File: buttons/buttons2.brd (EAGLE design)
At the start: 73 x 44 mm, 14 parts, among them U1 attiny2313

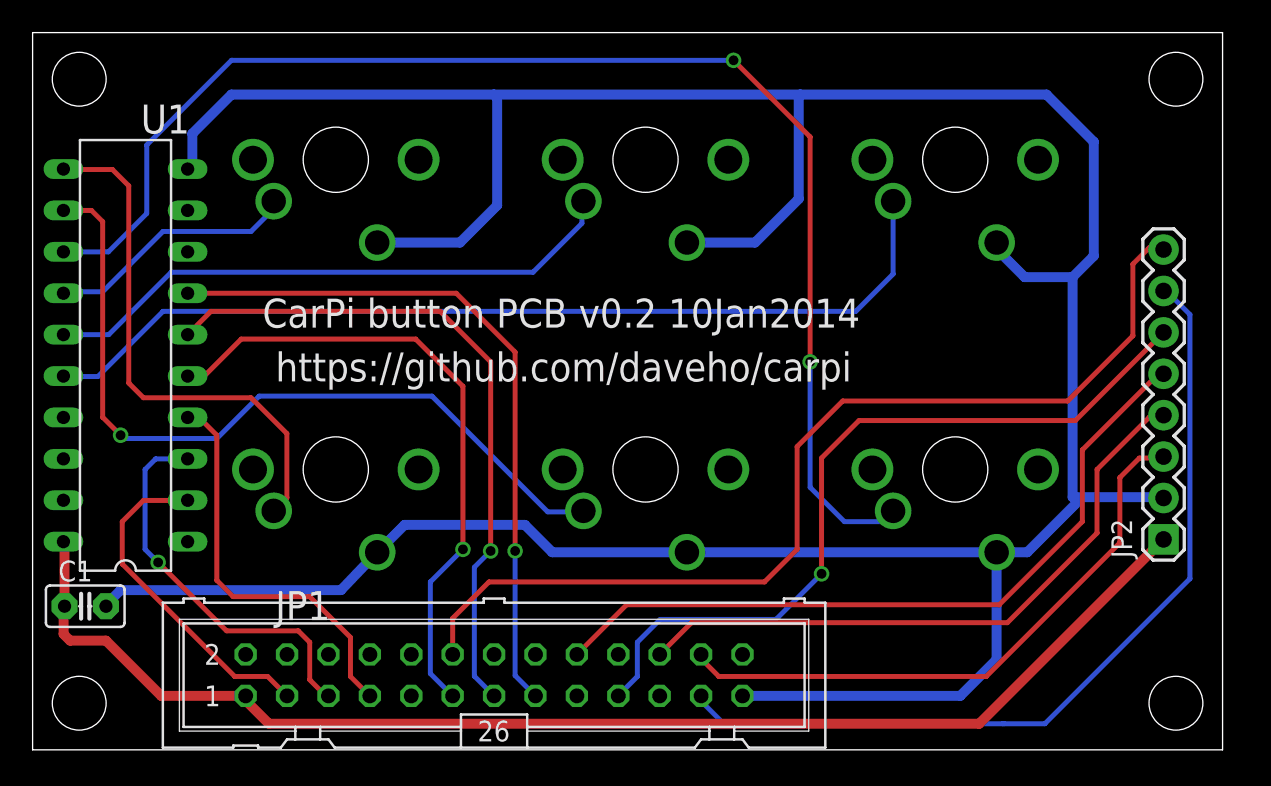
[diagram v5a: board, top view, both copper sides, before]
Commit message: updated buttons2/plate drawing for 19mm keycap
Made the PCB 74mm rather than 73mm to allow more space
between button cutout and button PCB screw hole.
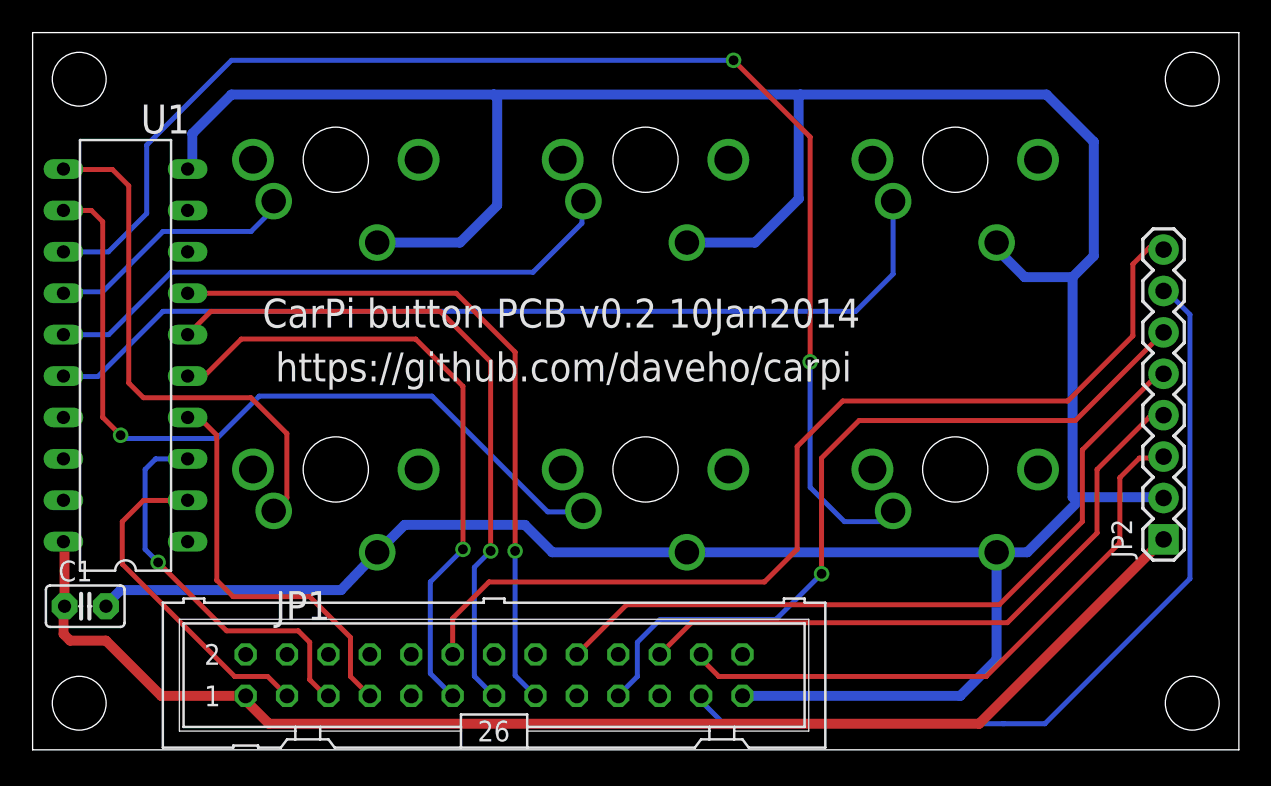
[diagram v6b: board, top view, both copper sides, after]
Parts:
- moved STANDOFF1 1.00 mm to (71.1, 2.86)
- moved STANDOFF3 1.00 mm to (71.1, 41.1)
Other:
- board size 73 x 44 mm -> 74 x 44 mm
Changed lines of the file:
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@@
 <board>
 <plain>
-<wire x1="0" y1="0" x2="73" y2="0" width="0" layer="20"/>
-<wire x1="73" y1="0" x2="73" y2="44" width="0" layer="20"/>
-<wire x1="73" y1="44" x2="0" y2="44" width="0" layer="20"/>
+<wire x1="0" y1="0" x2="74" y2="0" width="0" layer="20"/>
+<wire x1="74" y1="0" x2="74" y2="44" width="0" layer="20"/>
+<wire x1="74" y1="44" x2="0" y2="44" width="0" layer="20"/>
 <wire x1="0" y1="44" x2="0" y2="0" width="0" layer="20"/>
 <text x="14.1" y="25.9" size="1.778" layer="21" font="vector">CarPi button PCB v0.2 10Jan2014</text>
@@
 <attribute name="VALUE" x="0.679" y="6.016" size="1.27" layer="27" font="vector" ratio="10"/>
 </element>
-<element name="STANDOFF1" library="SparkFun-Electromechanical" package="STAND-OFF" value="STAND-OFF" x="70.14" y="2.86"/>
+<element name="STANDOFF1" library="SparkFun-Electromechanical" package="STAND-OFF" value="STAND-OFF" x="71.14" y="2.86"/>
 <element name="STANDOFF2" library="SparkFun-Electromechanical" package="STAND-OFF" value="STAND-OFF" x="2.86" y="2.86"/>
-<element name="STANDOFF3" library="SparkFun-Electromechanical" package="STAND-OFF" value="STAND-OFF" x="70.14" y="41.14"/>
+<element name="STANDOFF3" library="SparkFun-Electromechanical" package="STAND-OFF" value="STAND-OFF" x="71.14" y="41.14"/>
 <element name="STANDOFF4" library="SparkFun-Electromechanical" package="STAND-OFF" value="STAND-OFF" x="2.86" y="41.14"/>
 <element name="S1" library="cherrymx" package="CHERRY-MX-I" value="CHERRY-MX-I" x="18.6" y="17.2" rot="MR180"/>
@@
 <wire x1="5.4" y1="19.3" x2="5.6" y2="19.1" width="0.3048" layer="16"/>
 <wire x1="5.6" y1="19.1" x2="11.3" y2="19.1" width="0.3048" layer="16"/>
-<wire x1="11.3" y1="19.1" x2="13.1" y2="19.1" width="0" layer="19" extent="1-16"/>
 <wire x1="24.5" y1="21.7" x2="31.6" y2="14.6" width="0.3048" layer="16"/>
 <wire x1="31.6" y1="14.6" x2="33.73" y2="14.6" width="0.3048" layer="16"/>

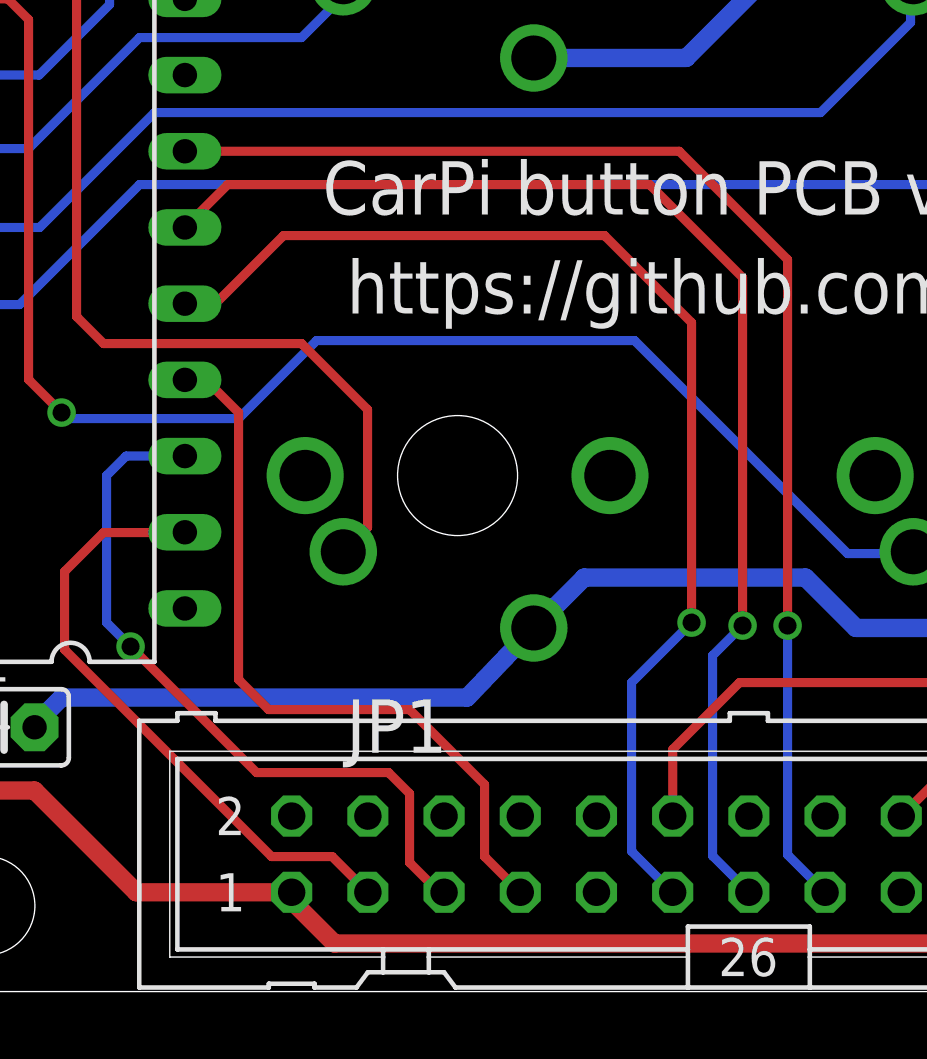
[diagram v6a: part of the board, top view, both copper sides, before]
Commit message: eliminated an unnecessary via
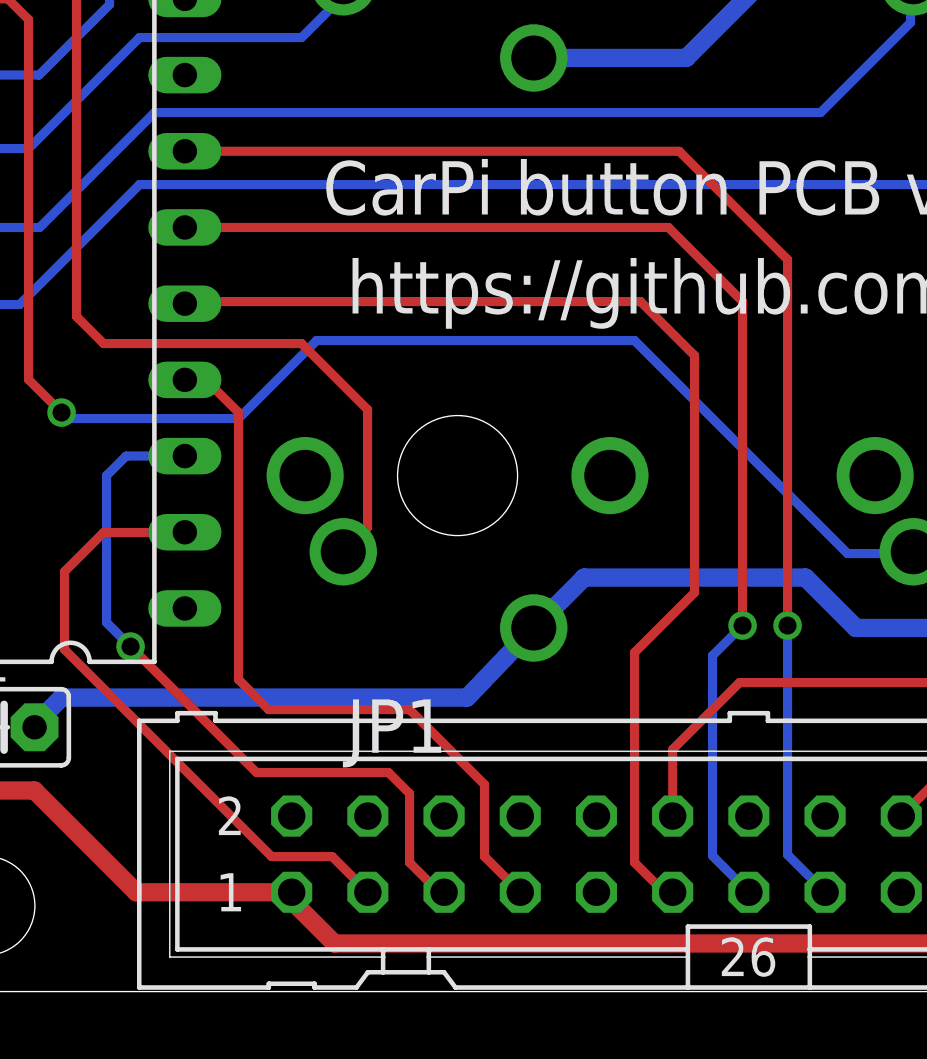
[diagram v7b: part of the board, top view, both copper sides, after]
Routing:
- net BUTTON4: track 39.4 -> 37.2 mm, vias 1 -> 0
- net BUTTON5: track 41.9 -> 40.2 mm
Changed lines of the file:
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@@
 <contactref element="JP1" pad="11"/>
 <contactref element="U1" pad="5"/>
-<wire x1="25.77" y1="3.31" x2="24.4" y2="4.68" width="0.3048" layer="16"/>
-<wire x1="24.4" y1="4.68" x2="24.4" y2="10.3" width="0.3048" layer="16"/>
-<wire x1="24.4" y1="10.3" x2="26.4" y2="12.3" width="0.3048" layer="16"/>
-<via x="26.4" y="12.3" extent="1-16" drill="0.6"/>
-<wire x1="9.51" y1="22.93" x2="10.53" y2="22.93" width="0.3048" layer="1"/>
-<wire x1="10.53" y1="22.93" x2="12.8" y2="25.2" width="0.3048" layer="1"/>
-<wire x1="12.8" y1="25.2" x2="23.5" y2="25.2" width="0.3048" layer="1"/>
-<wire x1="23.5" y1="25.2" x2="26.4" y2="22.3" width="0.3048" layer="1"/>
-<wire x1="26.4" y1="22.3" x2="26.4" y2="12.3" width="0.3048" layer="1"/>
+<wire x1="9.51" y1="22.93" x2="9.51" y2="22.99" width="0.3048" layer="1"/>
+<wire x1="9.51" y1="22.99" x2="9.5" y2="23" width="0.3048" layer="1"/>
+<wire x1="9.5" y1="23" x2="24.7" y2="23" width="0.3048" layer="1"/>
+<wire x1="24.7" y1="23" x2="26.5" y2="21.2" width="0.3048" layer="1"/>
+<wire x1="26.5" y1="21.2" x2="26.5" y2="13.3" width="0.3048" layer="1"/>
+<wire x1="25.77" y1="3.31" x2="25.49" y2="3.31" width="0.3048" layer="1"/>
+<wire x1="25.49" y1="3.31" x2="24.5" y2="4.3" width="0.3048" layer="1"/>
+<wire x1="24.5" y1="4.3" x2="24.5" y2="11.3" width="0.3048" layer="1"/>
+<wire x1="24.5" y1="11.3" x2="26.5" y2="13.3" width="0.3048" layer="1"/>
 </signal>
 <signal name="BUTTON5">
@@
 <wire x1="27.1" y1="11.2" x2="28.1" y2="12.2" width="0.3048" layer="16"/>
 <via x="28.1" y="12.2" extent="1-16" drill="0.6"/>
-<wire x1="9.51" y1="25.47" x2="10.94" y2="26.9" width="0.3048" layer="1"/>
-<wire x1="10.94" y1="26.9" x2="25" y2="26.9" width="0.3048" layer="1"/>
-<wire x1="25" y1="26.9" x2="28.1" y2="23.8" width="0.3048" layer="1"/>
-<wire x1="28.1" y1="23.8" x2="28.1" y2="12.2" width="0.3048" layer="1"/>
+<wire x1="28.1" y1="23.8" x2="28.1" y2="23" width="0" layer="19" extent="1-16"/>
+<wire x1="28.1" y1="23" x2="28.1" y2="12.2" width="0.3048" layer="1"/>
+<wire x1="9.51" y1="25.47" x2="25.63" y2="25.47" width="0.3048" layer="1"/>
+<wire x1="25.63" y1="25.47" x2="28.1" y2="23" width="0.3048" layer="1"/>
 </signal>
 <signal name="BUTTON6">

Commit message: a few more routing improvements
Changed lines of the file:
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@@
 <contactref element="S6" pad="PIN-1"/>
 <contactref element="U1" pad="16"/>
-<wire x1="52.79" y1="29.19" x2="50.5" y2="26.9" width="0.3048" layer="16"/>
-<wire x1="50.5" y1="26.9" x2="8" y2="26.9" width="0.3048" layer="16"/>
+<wire x1="52.79" y1="29.19" x2="50.35" y2="26.75" width="0.3048" layer="16"/>
 <wire x1="4" y1="22.9" x2="1.92" y2="22.9" width="0.3048" layer="16"/>
 <wire x1="1.92" y1="22.9" x2="1.89" y2="22.93" width="0.3048" layer="16"/>
-<wire x1="8" y1="26.9" x2="4" y2="22.9" width="0.3048" layer="16"/>
+<wire x1="8" y1="26.9" x2="7.85" y2="26.75" width="0" layer="19" extent="1-16"/>
+<wire x1="7.85" y1="26.75" x2="4" y2="22.9" width="0.3048" layer="16"/>
 <wire x1="52.79" y1="33.66" x2="52.79" y2="29.19" width="0.3048" layer="16"/>
+<wire x1="50.35" y1="26.75" x2="7.85" y2="26.75" width="0.3048" layer="16"/>
 </signal>
 <signal name="N$2">
@@
 <wire x1="48.4" y1="10.8" x2="45.6" y2="8" width="0.3048" layer="16"/>
 <wire x1="45.6" y1="8" x2="38.5" y2="8" width="0.3048" layer="16"/>
-<wire x1="38.5" y1="8" x2="37.1" y2="6.6" width="0.3048" layer="16"/>
-<wire x1="37.1" y1="6.6" x2="37.1" y2="4.5" width="0.3048" layer="16"/>
-<wire x1="37.1" y1="4.5" x2="35.93" y2="3.33" width="0.3048" layer="16"/>
+<wire x1="37.2" y1="4.6" x2="35.93" y2="3.33" width="0.3048" layer="16"/>
 <wire x1="35.93" y1="3.33" x2="35.93" y2="3.31" width="0.3048" layer="16"/>
+<wire x1="37.2" y1="4.6" x2="37.2" y2="6.7" width="0.3048" layer="16"/>
+<wire x1="37.2" y1="6.7" x2="38.5" y2="8" width="0.3048" layer="16"/>
 </signal>
 <signal name="SCK">
@@
 <contactref element="JP1" pad="23"/>
 <wire x1="69.38" y1="28.15" x2="69.55" y2="28.15" width="0.3048" layer="16"/>
-<wire x1="69.55" y1="28.15" x2="71" y2="26.7" width="0.3048" layer="16"/>
-<wire x1="71" y1="26.7" x2="71" y2="10.5" width="0.3048" layer="16"/>
+<wire x1="69.55" y1="28.15" x2="71.5" y2="26.2" width="0.3048" layer="16"/>
 <wire x1="41.01" y1="3.31" x2="41.01" y2="2.99" width="0.3048" layer="16"/>
 <wire x1="41.01" y1="2.99" x2="42.4" y2="1.6" width="0.3048" layer="16"/>
-<wire x1="42.4" y1="1.6" x2="59.5" y2="1.6" width="0.3048" layer="16"/>
-<wire x1="59.5" y1="1.6" x2="59.6" y2="1.6" width="0.3048" layer="16"/>
-<wire x1="71" y1="10.5" x2="62.1" y2="1.6" width="0.3048" layer="16"/>
-<wire x1="62.1" y1="1.6" x2="59.6" y2="1.6" width="0.3048" layer="16"/>
+<wire x1="42.4" y1="1.6" x2="62.1" y2="1.6" width="0.3048" layer="16"/>
+<wire x1="71.5" y1="11" x2="62.1" y2="1.6" width="0.3048" layer="16"/>
+<wire x1="71.5" y1="26.2" x2="71.5" y2="11" width="0.3048" layer="16"/>
 </signal>
 <signal name="BUTTON1">
@@
 <wire x1="27.1" y1="11.2" x2="28.1" y2="12.2" width="0.3048" layer="16"/>
 <via x="28.1" y="12.2" extent="1-16" drill="0.6"/>
-<wire x1="28.1" y1="23.8" x2="28.1" y2="23" width="0" layer="19" extent="1-16"/>
 <wire x1="28.1" y1="23" x2="28.1" y2="12.2" width="0.3048" layer="1"/>
 <wire x1="9.51" y1="25.47" x2="25.63" y2="25.47" width="0.3048" layer="1"/>
